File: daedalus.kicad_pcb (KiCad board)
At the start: 4 copper layers, 50 x 50 mm, 50 parts, among them J1 Power Input, J10 Left GPIO Pins, J11 UART 2, J12 Bottom GPIO Pins, J13 Right GPIO Pins, J2 Power Breakout, J3 I2C Out 0, J4 I2C Out 1, J5 I2C Out 1, J6 UART 0, J7 UART 1, J9 SWD Conn, SW1 SW_SPDT, U1 STM32F405RGTx, U2 AMS1117-3.3, Y1 16MHz

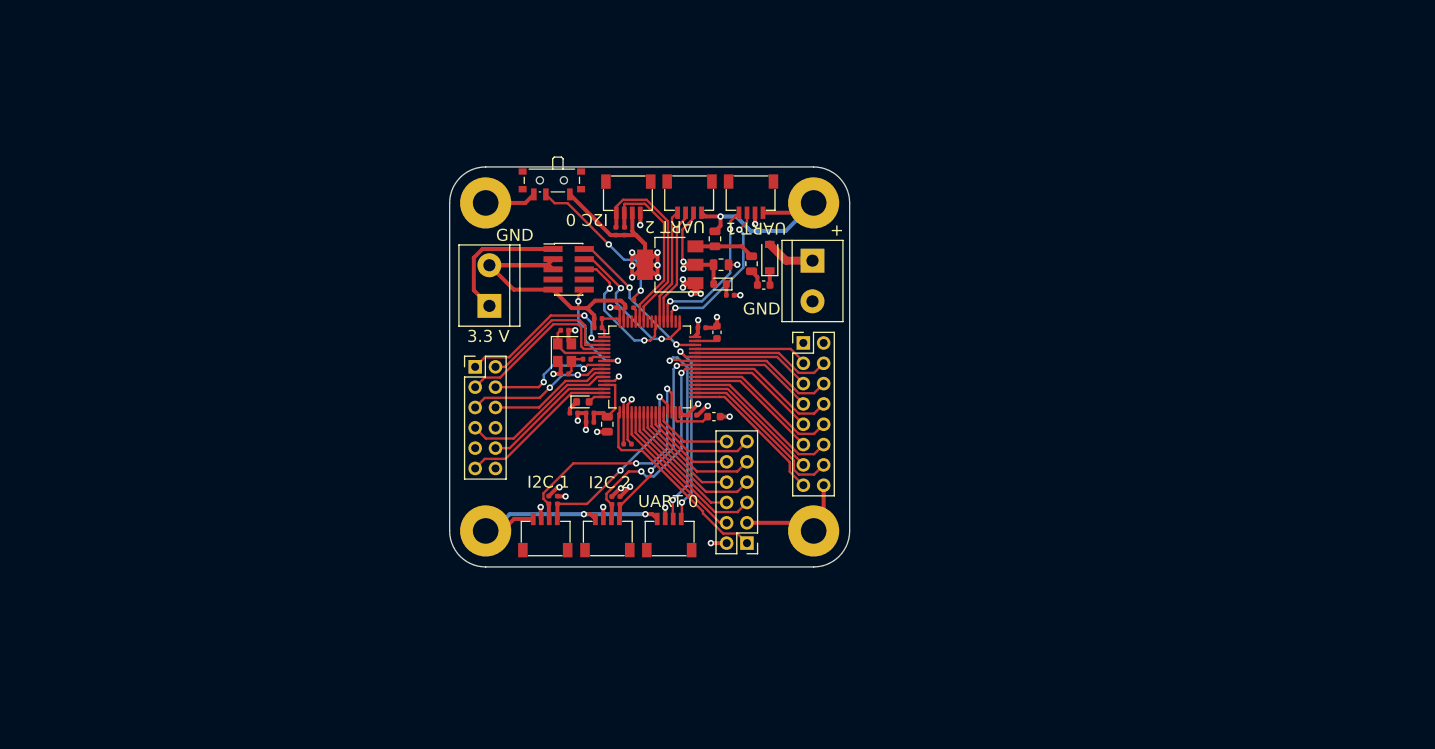
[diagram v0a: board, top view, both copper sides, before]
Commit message: Added footprints and side headers
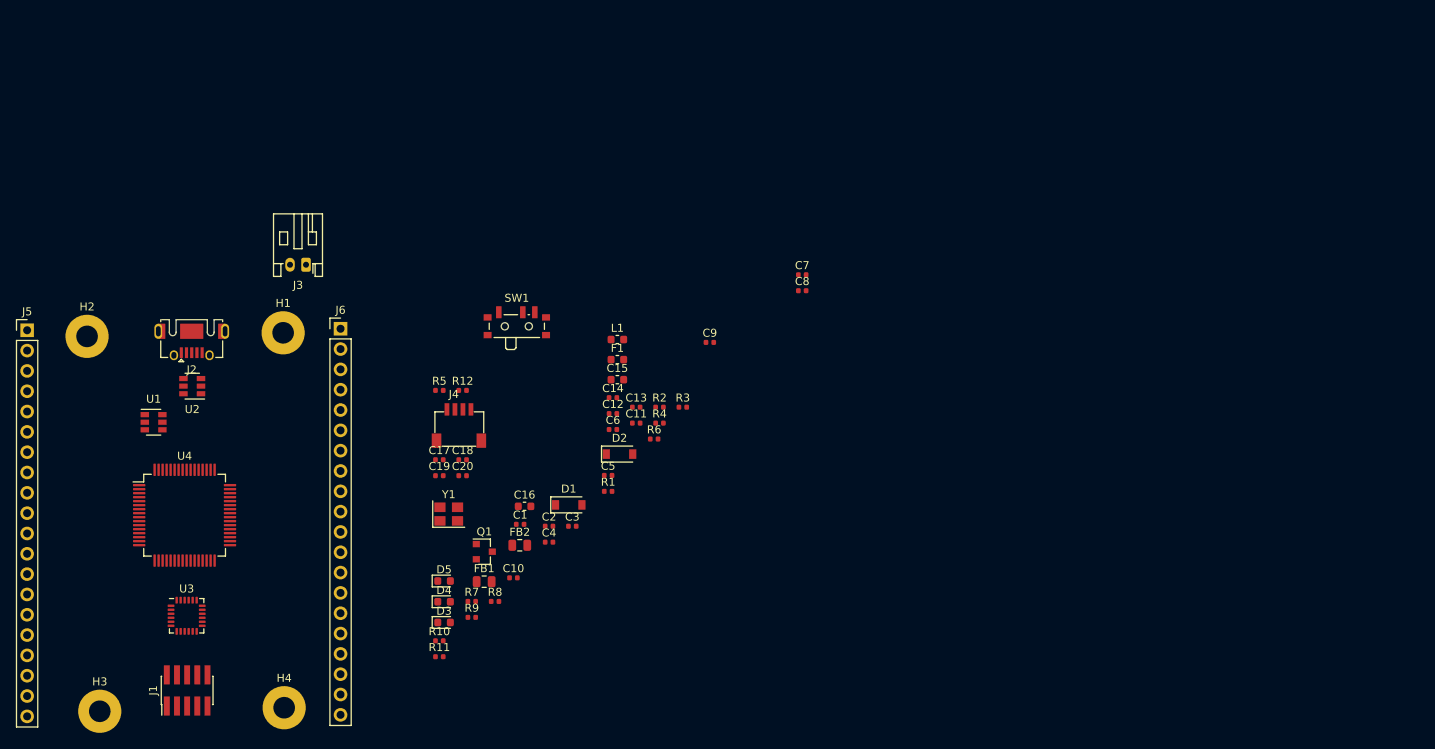
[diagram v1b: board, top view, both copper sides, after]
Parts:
- removed J10: Left GPIO Pins, Connector_PinHeader_2.54mm:PinHeader_2x06_P2.54mm_Vertical
- removed J11: UART 2, Eric:JST_SH4
- removed J12: Bottom GPIO Pins, Connector_PinHeader_2.54mm:PinHeader_2x06_P2.54mm_Vertical
- removed J13: Right GPIO Pins, Connector_PinHeader_2.54mm:PinHeader_2x08_P2.54mm_Vertical
- removed J7: UART 1, Eric:JST_SH4
- removed J9: SWD Conn, Connector_PinHeader_1.27mm:PinHeader_2x05_P1.27mm_Vertical_SMD
- added C11: 1uF, Capacitor_SMD:C_0402_1005Metric, F.Cu at (143.3, 101.1)
- added C12: 10nF, Capacitor_SMD:C_0402_1005Metric, F.Cu at (140.4, 100.0)
- added C15: 2.2 uF, Capacitor_SMD:C_0603_1608Metric, F.Cu at (141.0, 95.7)
- added C18: 12 pF, Capacitor_SMD:C_0402_1005Metric, F.Cu at (121.6, 105.7)
- added C19: 100nF, Capacitor_SMD:C_0402_1005Metric, F.Cu at (118.7, 107.7)
- added C20: 2.2nF, Capacitor_SMD:C_0402_1005Metric, F.Cu at (121.6, 107.7)
- added D4: Blue, LED_SMD:LED_0603_1608Metric, F.Cu at (119.3, 123.5)
- added D5: Green, LED_SMD:LED_0603_1608Metric, F.Cu at (119.3, 120.9)
- added L1: 10uH, Inductor_SMD:L_0603_1608Metric, F.Cu at (141.0, 90.7)
- added Q1: AO3401A, Package_TO_SOT_SMD:SOT-23, F.Cu at (124.3, 117.2)
- added R11: 1k5, Resistor_SMD:R_0402_1005Metric, F.Cu at (118.7, 130.3)
- added R12: 1k5, Resistor_SMD:R_0402_1005Metric, F.Cu at (121.6, 97.1)
- added U3: MPU-6050, Sensor_Motion:InvenSense_QFN-24_4x4mm_P0.5mm, F.Cu at (87.1, 125.2)
- added U4: STM32F405RGTx, Package_QFP:LQFP-64_10x10mm_P0.5mm, F.Cu at (86.9, 112.6)
- C1: value 2.2 uF -> 10nF; footprint Capacitor_SMD:C_0603_1608Metric -> Capacitor_SMD:C_0402_1005Metric
- C10, C7: value 10 uF -> 100 nF; footprint Capacitor_SMD:C_0805_2012Metric -> Capacitor_SMD:C_0402_1005Metric
- C13: value 100 nF -> 100nF
- C14: value 12 pF -> 100nF
- C16: value 10 nF -> 2.2 uF; footprint Capacitor_SMD:C_0402_1005Metric -> Capacitor_SMD:C_0603_1608Metric
- C2: value 4u7 -> 10uF
- C3: value 2.2 uF -> 10uF; footprint Capacitor_SMD:C_0603_1608Metric -> Capacitor_SMD:C_0402_1005Metric
- C4: value 100 nF -> 10uF
- C5: value 100 nF -> 4u7
- D2: value Green -> B5819W; footprint LED_SMD:LED_0603_1608Metric -> Diode_SMD:D_SOD-123
- F1: value 500 mAh -> 250mA
- FB1, FB2: value 100 @ 100 MHz -> 600 @ 600MHz
- H1, H2, H3, H4: footprint MountingHole:MountingHole_3.2mm_M3_Pad -> MountingHole:MountingHole_2.7mm_M2.5_Pad
- J1: value Power Input -> SWD; footprint TerminalBlock:TerminalBlock_bornier-2_P5.08mm -> Connector_PinHeader_1.27mm:PinHeader_2x05_P1.27mm_Vertical_SMD
- J2: value Power Breakout -> USB_B_Micro; footprint TerminalBlock:TerminalBlock_bornier-2_P5.08mm -> Connector_USB:USB_Micro-AB_Molex_47590-0001
- J3: value I2C Out 0 -> JST LiPo Input; footprint Eric:JST_SH4 -> Connector_JST:JST_PH_S2B-PH-K_1x02_P2.00mm_Horizontal
- J4: value I2C Out 1 -> I2C 1 Breakout
- J5: value I2C Out 1 -> Conn_01x20_Male; footprint Eric:JST_SH4 -> Connector_PinHeader_2.54mm:PinHeader_1x20_P2.54mm_Vertical
- J6: value UART 0 -> Conn_01x20_Male; footprint Eric:JST_SH4 -> Connector_PinHeader_2.54mm:PinHeader_1x20_P2.54mm_Vertical
- R1: value 10k -> 47k
- R10: value 2k2 -> 1k
- R2: value 2k2 -> 100K
- R3: value 1k5 -> 15k
- R4: value 2k2 -> 68K
- R5: value 2k2 -> 270
- R7: value 220 -> 2k2
- R8: value 1k5 -> 220
- R9: value 2k2 -> 10k
- U1: value STM32F405RGTx -> MP2359DJ-LF-Z; footprint Package_QFP:LQFP-64_10x10mm_P0.5mm -> Package_TO_SOT_SMD:SOT-23-6
- U2: value AMS1117-3.3 -> USBLC6-2SC6; footprint Package_TO_SOT_SMD:SOT-223-3_TabPin2 -> Package_TO_SOT_SMD:SOT-23-6
- moved J1 94.8 mm to (87.2, 134.6), turned to 90 degrees
- moved H2 92.3 mm to (74.7, 90.3)
- moved H3 79.8 mm to (76.3, 137.2)
- moved J5 77.1 mm to (67.2, 89.5)
- moved H4 69.8 mm to (99.3, 136.7)
- moved U1 62.4 mm to (83.0, 101.0)
- moved U2 61.7 mm to (87.8, 96.5)
- moved FB1 51.9 mm to (124.3, 121.0), turned to 0 degrees
- moved J6 48.8 mm to (106.4, 89.3)
- moved C10 47.0 mm to (128.0, 120.5), turned to 0 degrees
- moved J3 41.3 mm to (102.0, 81.3)
- moved D1 39.8 mm to (134.9, 111.4), turned to 0 degrees
- moved J2 37.3 mm to (87.8, 89.7), turned to 180 degrees
- moved H1 35.4 mm to (99.2, 89.9)
- moved R7 33.5 mm to (122.8, 123.4), turned to 0 degrees
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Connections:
- C1 pad 1: GND -> BUCK_SW
- C1 pad 2: Net-(C1-Pad2) -> BUCK_BST
- C13 pad 1: GND -> +3V3
- C13 pad 2: +3.3VA -> GND
- C14 pad 1: GND -> +3V3
- C14 pad 2: HSE_IN -> GND
- C16 pad 2: +3.3VA -> Net-(C16-Pad2)
- C17 pad 2: Net-(C17-Pad2) -> HSE_IN
- C2 pad 1: GND -> Net-(C2-Pad1)
- C2 pad 2: +3V3 -> GND
- C3 pad 2: Net-(C3-Pad2) -> +3V3
- C7 pad 2: Net-(C7-Pad2) -> +3V3
- D1 pad 2: VCC -> +5V
- D2 pad 1: Net-(D2-Pad1) -> BUCK_SW
- D2 pad 2: +3V3 -> GND
- D3 pad 2: LED_STATUS -> Net-(D3-Pad2)
- F1 pad 1: Net-(D1-Pad1) -> Net-(F1-Pad1)
- F1 pad 2: Net-(F1-Pad2) -> VCC
- FB1 pad 1: Net-(C7-Pad2) -> Net-(C2-Pad1)
- FB1 pad 2: Net-(F1-Pad2) -> Net-(D1-Pad1)
- J2 pad : GND -> (no net)
- J3 pad 1: GND -> +3V3
- J3 pad 2: +3V3 -> GND
- J4 pad 3: I2C_1_SDA -> I2C1_SDA
- J4 pad 4: I2C_1_SCL -> I2C1_SCL
- J5 pad 1: GND -> GPIO_PB5
- J5 pad 2: +3V3 -> GPIO_PB8
- J5 pad 3: I2C_2_SDA -> GPIO_PB9
- J5 pad 4: I2C_2_SCL -> GPIO_PC13
- J6 pad 1: GND -> GPIO_PB4
- J6 pad 2: +3V3 -> GPIO_PD2
- J6 pad 3: UART_0_TX -> GPDIO_PC12
- J6 pad 4: UART_0_RX -> GPIO_PC11
- R1 pad 1: Net-(R1-Pad1) -> +3V3
- R1 pad 2: BOOT0 -> BUCK_FB
- R10 pad 1: +3V3 -> Net-(D3-Pad1)
- R10 pad 2: I2C_2_SDA -> GND
- R2 pad 1: +3V3 -> Net-(C2-Pad1)
- R2 pad 2: I2C_0_SCL -> Net-(R2-Pad2)
- R3 pad 1: Net-(D2-Pad1) -> BUCK_FB
- R3 pad 2: GND -> Net-(R3-Pad2)
- R4 pad 1: +3V3 -> Net-(R2-Pad2)
- R4 pad 2: I2C_0_SDA -> GND
- R5 pad 1: +3V3 -> Net-(R3-Pad2)
- R5 pad 2: I2C_1_SCL -> GND
- R6 pad 2: I2C_1_SDA -> I2C1_SCL
- R7 pad 1: HSE_OUT -> +3V3
- R7 pad 2: Net-(C17-Pad2) -> I2C1_SDA
- R8 pad 1: GND -> HSE_OUT
- R8 pad 2: Net-(D3-Pad1) -> Net-(C18-Pad2)
- R9 pad 1: +3V3 -> Net-(D3-Pad2)
- R9 pad 2: I2C_2_SCL -> BOOT0
- SW1 pad 2: Net-(R1-Pad1) -> Net-(D3-Pad2)
- U1 pad 1: +3V3 -> BUCK_BST
- U1 pad 2: GPIO_PC13 -> GND
- U1 pad 3: GPIO_PC14 -> BUCK_FB
- U1 pad 4: GPIO_PC15 -> Net-(R2-Pad2)
- U1 pad 5: HSE_IN -> Net-(C2-Pad1)
- U1 pad 6: HSE_OUT -> BUCK_SW
- U2 pad 1: GND -> USB_CONN_D-
- U2 pad 2: +3V3 -> GND
- U2 pad 3: Net-(C7-Pad2) -> USB_CONN_D+
- Y1 pad 3: Net-(C17-Pad2) -> Net-(C18-Pad2)
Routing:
- net GND: track 155.2 -> 0.00 mm, vias 19 -> 0
- net +3V3: track 107.4 -> 0.00 mm, vias 22 -> 0
- net I2C_2_SDA: track 46.0 -> 0.00 mm, vias 2 -> 0
- net UART_0_TX: track 44.1 -> 0.00 mm, vias 2 -> 0
- net I2C_2_SCL: track 40.1 -> 0.00 mm, vias 2 -> 0
- net UART_0_RX: track 39.1 -> 0.00 mm, vias 2 -> 0
- net I2C_1_SDA: track 32.0 -> 0.00 mm, vias 2 -> 0
- net AIN_3: track 25.6 -> 0.00 mm
- net I2C_1_SCL: track 25.1 -> 0.00 mm, vias 2 -> 0
- net I2C_0_SCL: track 24.3 -> 0.00 mm
- net I2C_0_SDA: track 22.5 -> 0.00 mm
- net GPIO_PC15: track 22.1 -> 0.00 mm
- net GPIO_PB13: track 21.5 -> 0.00 mm
- net GPIO_PC13: track 21.2 -> 0.00 mm, vias 2 -> 0
- net GPIO_PA5: track 21.1 -> 0.00 mm
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- removed copper zone on In2.Cu, net +3V3
- removed copper zone on In1.Cu, net GND
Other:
- board size 50 x 50 mm -> 7.5 x 2 mm
- copper layers 4 -> 2
- board text removed: "+"
- board text removed: "3.3 V"
- board text removed: "GND"
- board text removed: "I2C 0"
- board text removed: "I2C 1"
- board text removed: "I2C 2"
- board text removed: "Jeremy Kanovsky Spring 2021 STM32F405RGT6 Breakout v1.0"
- board text removed: "UART 0"
- board text removed: "UART 1"
- board text removed: "UART 2"

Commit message: Began board layout
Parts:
- added C21: 1uF, 50V, Capacitor_SMD:C_0402_1005Metric, F.Cu at (122.4, 92.9)
- added C22: 22uF, 10V, Capacitor_SMD:C_0402_1005Metric, F.Cu at (130.5, 75.9)
- added C23: 0.1uF, 10V, Capacitor_SMD:C_0603_1608Metric, F.Cu at (129.9, 67.3)
- added C24: 0.1uF, 10V, Capacitor_SMD:C_0603_1608Metric, F.Cu at (123.3, 67.3)
- added C25: 12 pF, Capacitor_SMD:C_0402_1005Metric, F.Cu at (133.3, 72.3)
- added C26: 12 pF, Capacitor_SMD:C_0402_1005Metric, F.Cu at (132.9, 77.7)
- added C27: 0.1uF, 10V, Capacitor_SMD:C_0402_1005Metric, F.Cu at (123.4, 94.9)
- added C28: 10uF, 50V, Capacitor_SMD:C_1206_3216Metric, F.Cu at (115.6, 89.5)
- added C29: 10uF, 50V, Capacitor_SMD:C_1206_3216Metric, F.Cu at (144.5, 108.0)
- added C30: 10uF, 50V, Capacitor_SMD:C_1206_3216Metric, F.Cu at (142.2, 103.3)
- added C31: 10uF, 50V, Capacitor_SMD:C_1206_3216Metric, F.Cu at (146.9, 108.0)
- added C32: 10uF, 50V, Capacitor_SMD:C_1206_3216Metric, F.Cu at (90.6, 66.1)
- added C33: 10uF, 50V, Capacitor_SMD:C_1206_3216Metric, F.Cu at (90.6, 69.4)
- added C34: 10uF, 50V, Capacitor_SMD:C_1206_3216Metric, F.Cu at (115.6, 91.9)
- added C35: 10uF, 50V, Capacitor_SMD:C_1206_3216Metric, F.Cu at (115.6, 69.3)
- added C36: 10uF, 50V, Capacitor_SMD:C_1206_3216Metric, F.Cu at (142.2, 108.0)
- added C37: 10uF, 50V, Capacitor_SMD:C_1206_3216Metric, F.Cu at (115.6, 78.3)
- added C38: 10uF, 50V, Capacitor_SMD:C_1206_3216Metric, F.Cu at (146.9, 103.3)
- added C39: 10uF, 50V, Capacitor_SMD:C_1206_3216Metric, F.Cu at (139.8, 103.3)
- added C40: 10uF, 50V, Capacitor_SMD:C_1206_3216Metric, F.Cu at (115.6, 66.9)
- added C41: 10uF, 50V, Capacitor_SMD:C_1206_3216Metric, F.Cu at (144.5, 103.3)
- added C42: 10uF, 50V, Capacitor_SMD:C_1206_3216Metric, F.Cu at (139.8, 108.0)
- added C43: 10uF, 50V, Capacitor_SMD:C_1206_3216Metric, F.Cu at (115.6, 80.6)
- added D6: Blue, LED_SMD:LED_0603_1608Metric, F.Cu at (156.6, 82.8)
- added D7: Green, LED_SMD:LED_0603_1608Metric, F.Cu at (156.6, 79.5)
- added J7: C Terminal, daedalus_kicad_lib:18_AWG_PAD, F.Cu at (97.9, 96.9)
- added J8: SWD, Connector_PinHeader_1.27mm:PinHeader_2x05_P1.27mm_Vertical_SMD, F.Cu at (162.0, 91.6)
- added J9: USB_B_Micro, Connector_USB:USB_Micro-AB_Molex_47590-0001, F.Cu at (163.0, 101.3)
- added L2: 22uH, Inductor_SMD:L_0603_1608Metric, F.Cu at (127.3, 80.3)
- added R13: 54.9k, Resistor_SMD:R_0402_1005Metric, F.Cu at (122.2, 78.0)
- added R14: 10k, Resistor_SMD:R_0402_1005Metric, F.Cu at (121.6, 79.8)
- added R15: 10k, Resistor_SMD:R_0402_1005Metric, F.Cu at (154.1, 81.2)
- added R16: 1k, Resistor_SMD:R_0402_1005Metric, F.Cu at (159.2, 81.2)
- added R17: 1k5, Resistor_SMD:R_0402_1005Metric, F.Cu at (159.2, 82.9)
- added R18: 1k5, Resistor_SMD:R_0402_1005Metric, F.Cu at (159.2, 79.6)
- added R19: 0.001, Resistor_SMD:R_0402_1005Metric, F.Cu at (118.0, 83.4)
- added R20: 0.001, Resistor_SMD:R_0402_1005Metric, F.Cu at (117.8, 87.5)
- added R21: 0.001, Resistor_SMD:R_0402_1005Metric, F.Cu at (120.6, 90.9)
- added U10: TPH, daedalus_kicad_lib:TRANS_TPH5900CNH,L1Q, F.Cu at (109.4, 90.7)
- added U11: TPH, daedalus_kicad_lib:TRANS_TPH5900CNH,L1Q, F.Cu at (109.4, 73.8)
- added U12: TPH, daedalus_kicad_lib:TRANS_TPH5900CNH,L1Q, F.Cu at (109.4, 85.1)
- added U13: TPH, daedalus_kicad_lib:TRANS_TPH5900CNH,L1Q, F.Cu at (109.4, 96.4)
- added U14: USBLC6-2SC6, Package_TO_SOT_SMD:SOT-23-6, F.Cu at (157.0, 101.3)
- added U5: DRV8323RH, daedalus_kicad_lib:QFN50P700X700X90-49N, F.Cu at (123.4, 85.5)
- added U6: MCP2542, daedalus_kicad_lib:TDFN, F.Cu at (125.3, 68.1)
- added U7: STM32F405RGTx, Package_QFP:LQFP-64_10x10mm_P0.5mm, F.Cu at (142.7, 76.0)
- added U8: TPH, daedalus_kicad_lib:TRANS_TPH5900CNH,L1Q, F.Cu at (109.4, 68.1)
- added U9: TPH, daedalus_kicad_lib:TRANS_TPH5900CNH,L1Q, F.Cu at (109.4, 79.4)
- C11: value 1uF -> 0.1uF, 10V; footprint Capacitor_SMD:C_0402_1005Metric -> Capacitor_SMD:C_0603_1608Metric
- C12: value 10nF -> 1uF
- C13: value 100nF -> 10nF
- C14: value 100nF -> 10uF 50V; footprint Capacitor_SMD:C_0402_1005Metric -> Capacitor_SMD:C_1206_3216Metric
- C15: value 2.2 uF -> 0.1 uF 50V; footprint Capacitor_SMD:C_0603_1608Metric -> Capacitor_SMD:C_0402_1005Metric
- C16: value 2.2 uF -> 47nF, 50V; footprint Capacitor_SMD:C_0603_1608Metric -> Capacitor_SMD:C_0402_1005Metric
- C17: value 12 pF -> 1uF, 10V
- C18: value 12 pF -> 0.1uF, 50V
- C19: value 100nF -> 2.2 uF; footprint Capacitor_SMD:C_0402_1005Metric -> Capacitor_SMD:C_0603_1608Metric
- C20: value 2.2nF -> 2.2 uF; footprint Capacitor_SMD:C_0402_1005Metric -> Capacitor_SMD:C_0603_1608Metric
- D3: value Red -> B5819W; footprint LED_SMD:LED_0603_1608Metric -> Diode_SMD:D_SOD-123
- D4: value Blue -> 500mA, 60V; footprint LED_SMD:LED_0603_1608Metric -> Diode_SMD:D_SOD-123
- D5: value Green -> Red
- J1: value SWD -> CAN Bus; footprint Connector_PinHeader_1.27mm:PinHeader_2x05_P1.27mm_Vertical_SMD -> Connector_JST:JST_PH_S3B-PH-K_1x03_P2.00mm_Horizontal
- J2: value USB_B_Micro -> CAN Bus; footprint Connector_USB:USB_Micro-AB_Molex_47590-0001 -> Connector_JST:JST_PH_S3B-PH-K_1x03_P2.00mm_Horizontal
- J3: value JST LiPo Input -> I2C 1 Breakout; footprint Connector_JST:JST_PH_S2B-PH-K_1x02_P2.00mm_Horizontal -> Connector_JST:JST_PH_S4B-PH-K_1x04_P2.00mm_Horizontal
- J4: footprint Eric:JST_SH4 -> Connector_JST:JST_PH_S4B-PH-K_1x04_P2.00mm_Horizontal
- J5: value Conn_01x20_Male -> A Terminal; footprint Connector_PinHeader_2.54mm:PinHeader_1x20_P2.54mm_Vertical -> daedalus_kicad_lib:18_AWG_PAD
- J6: value Conn_01x20_Male -> B Terminal; footprint Connector_PinHeader_2.54mm:PinHeader_1x20_P2.54mm_Vertical -> daedalus_kicad_lib:18_AWG_PAD
- R10: value 1k -> 2k2
- R11: value 1k5 -> 2k2
- R12: value 1k5 -> 220
- R6, R7: value 2k2 -> 10k
- R8: value 220 -> 2k2
- R9: value 10k -> 2k2
- U1: value MP2359DJ-LF-Z -> XT30; footprint Package_TO_SOT_SMD:SOT-23-6 -> daedalus_kicad_lib:XT30_HORIZONTAL; moved to B.Cu
- U2: value USBLC6-2SC6 -> XT30; footprint Package_TO_SOT_SMD:SOT-23-6 -> daedalus_kicad_lib:XT30_HORIZONTAL; moved to B.Cu
- U3: value MPU-6050 -> MP2359DJ-LF-Z; footprint Sensor_Motion:InvenSense_QFN-24_4x4mm_P0.5mm -> Package_TO_SOT_SMD:SOT-23-6
- U4: value STM32F405RGTx -> MA700; footprint Package_QFP:LQFP-64_10x10mm_P0.5mm -> daedalus_kicad_lib:QFN16
- moved U4 134.7 mm to (219.4, 88.9)
- moved H4 96.7 mm to (159.6, 61.1)
- moved J1 84.7 mm to (133.3, 63.6), turned to 180 degrees
- moved H3 84.0 mm to (154.8, 107.4)
- moved C11 73.0 mm to (215.5, 89.7)
- moved R11 68.0 mm to (140.9, 66.0), turned to 180 degrees
- moved U3 67.3 mm to (141.6, 85.7)
- moved R10 65.5 mm to (138.9, 66.0), turned to 180 degrees
- moved R9 63.1 mm to (156.5, 72.0), turned to 90 degrees
- moved R8 61.7 mm to (156.5, 70.0), turned to 90 degrees
- moved U2 55.6 mm to (143.4, 98.4), turned to 0 degrees
- moved D5 54.5 mm to (156.6, 81.2), turned to 180 degrees
- moved C10 53.6 mm to (149.1, 71.2), turned to 180 degrees
- moved D4 49.9 mm to (127.6, 74.2)
- moved U1 47.3 mm to (130.2, 98.4)
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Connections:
- net INT_ACC renamed Net-(U4-Pad10)
- net INT_GYR renamed Net-(U4-Pad11)
- C10 pad 1: GND -> BGND
- C10 pad 2: +3V3 -> VDD
- C11 pad 1: GND -> VDD
- C11 pad 2: +3.3VA -> BGND
- C12 pad 1: GND -> BGND
- C13 pad 1: +3V3 -> BGND
- C13 pad 2: GND -> +3.3VA
- C14 pad 1: +3V3 -> BGND
- C14 pad 2: GND -> VIN
- C15 pad 1: GND -> BGND
- C15 pad 2: Net-(C15-Pad2) -> VIN
- C16 pad 1: GND -> Net-(C16-Pad1)
- C17 pad 1: GND -> BGND
- C17 pad 2: HSE_IN -> Net-(C17-Pad2)
- C18 pad 1: GND -> CB
- C18 pad 2: Net-(C18-Pad2) -> SW
- C19 pad 1: Net-(C19-Pad1) -> BGND
- C19 pad 2: GND -> Net-(C19-Pad2)
- C2 pad 2: GND -> BGND
- C20 pad 1: Net-(C20-Pad1) -> BGND
- C20 pad 2: GND -> Net-(C20-Pad2)
- C3 pad 1: GND -> BGND
- C3 pad 2: +3V3 -> VDD
- C4 pad 1: GND -> BGND
- C4 pad 2: +3V3 -> VDD
- C5 pad 1: GND -> BGND
- C5 pad 2: +3V3 -> VDD
- C6 pad 1: GND -> BGND
- C6 pad 2: +3V3 -> VDD
- C7 pad 1: GND -> BGND
- C7 pad 2: +3V3 -> VDD
- C8 pad 1: GND -> BGND
- C8 pad 2: +3V3 -> VDD
- C9 pad 1: GND -> BGND
- C9 pad 2: +3V3 -> VDD
- D1 pad 2: +5V -> +5VD
- D2 pad 1: BUCK_SW -> Net-(D2-Pad1)
- D2 pad 2: GND -> +5V
- D3 pad 1: Net-(D3-Pad1) -> BUCK_SW
- D3 pad 2: Net-(D3-Pad2) -> BGND
- D4 pad 1: Net-(D4-Pad1) -> SW
- D4 pad 2: LED_STATUS -> BGND
- D5 pad 2: +3V3 -> Net-(D5-Pad2)
- F1 pad 2: VCC -> Net-(D1-Pad1)
- FB1 pad 2: Net-(D1-Pad1) -> Net-(D2-Pad1)
- FB2 pad 2: +3V3 -> VDD
- H1 pad 1: GND -> BGND
- H2 pad 1: GND -> BGND
- H3 pad 1: GND -> BGND
- H4 pad 1: GND -> BGND
- J1 pad 1: +3V3 -> CANH
- J1 pad 2: SWDIO -> CANL
- J1 pad 3: GND -> BGND
- J2 pad 1: +5V -> CANH
- J2 pad 2: USB_CONN_D- -> CANL
- J2 pad 3: USB_CONN_D+ -> BGND
- J3 pad 1: +3V3 -> BGND
- J3 pad 2: GND -> VDD
- J4 pad 1: GND -> BGND
- J4 pad 2: +3V3 -> VDD
- L1 pad 2: +3V3 -> VDD
- Q1 pad 1: GND -> BGND
- Q1 pad 2: Net-(D1-Pad1) -> Net-(D2-Pad1)
- R1 pad 1: +3V3 -> VDD
- R10 pad 1: Net-(D3-Pad1) -> VDD
- R10 pad 2: GND -> I2C1_SCL
- R11 pad 1: GND -> VDD
- R11 pad 2: Net-(D4-Pad1) -> I2C1_SDA
- R12 pad 1: GND -> HSE_OUT
- R12 pad 2: Net-(D5-Pad1) -> Net-(C26-Pad2)
- R4 pad 2: GND -> BGND
- R5 pad 2: GND -> BGND
- R6 pad 1: +3V3 -> VDD
- R6 pad 2: I2C1_SCL -> SPI1_MISO
- R7 pad 1: +3V3 -> VDD
- R7 pad 2: I2C1_SDA -> FAULT
- R8 pad 1: HSE_OUT -> VDD
- R8 pad 2: Net-(C18-Pad2) -> I2C1_SCL
- R9 pad 1: Net-(D3-Pad2) -> VDD
- R9 pad 2: BOOT0 -> I2C1_SDA
- SW1 pad 1: +3V3 -> VDD
- SW1 pad 2: Net-(D3-Pad2) -> Net-(D5-Pad2)
- SW1 pad 3: GND -> BGND
- U3 pad 1: GND -> BUCK_BST
- U3 pad 2: (no net) -> BGND
- U3 pad 3: (no net) -> BUCK_FB
- U3 pad 4: (no net) -> Net-(R2-Pad2)
- U3 pad 5: (no net) -> Net-(C2-Pad1)
- U3 pad 6: Net-(U3-Pad6) -> BUCK_SW
- U4 pad 1: +3V3 -> Net-(U4-Pad1)
- U4 pad 12: GND -> SPI2_SCK
- U4 pad 13: +3.3VA -> VDD
- U4 pad 14: GPIO_PA0 -> Net-(U4-Pad14)
- U4 pad 15: GPIO_PA1 -> Net-(U4-Pad15)
- U4 pad 16: LED_STATUS -> Net-(U4-Pad16)
- U4 pad 2: GPIO_PC13 -> END_B
- U4 pad 3: GPIO_PC14 -> Net-(U4-Pad3)
- U4 pad 4: GPIO_PC15 -> SPI2_MOSI
- U4 pad 5: HSE_IN -> SPI2_CS
- U4 pad 6: HSE_OUT -> END_A
- U4 pad 7: NRST -> SPI2_MISO
- U4 pad 8: GPIO_PC0 -> BGND
- U4 pad 9: GPIO_PC1 -> Net-(U4-Pad9)
- Y1 pad 2: GND -> BGND
- Y1 pad 3: Net-(C18-Pad2) -> Net-(C26-Pad2)
- Y1 pad 4: GND -> BGND
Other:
- board size 7.5 x 2 mm -> 2 x 7.5 mm
- copper layers 2 -> 4
